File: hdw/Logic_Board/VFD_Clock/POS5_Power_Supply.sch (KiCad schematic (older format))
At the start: 0 parts

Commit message: Added +3.3V SW sheet
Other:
- note added: "LT8606? LT8607?"
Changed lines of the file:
@@
 EELAYER 29 0
 EELAYER END
-$Descr A4 11693 8268
+$Descr A 11000 8500
 encoding utf-8
-Sheet 1 21
+Sheet 20 22
 Title ""
 Date ""
@@
 Comment4 ""
 $EndDescr
+Text Notes 5040 3680 0    50   ~ 0
+LT8606? LT8607?
 $EndSCHEMATC

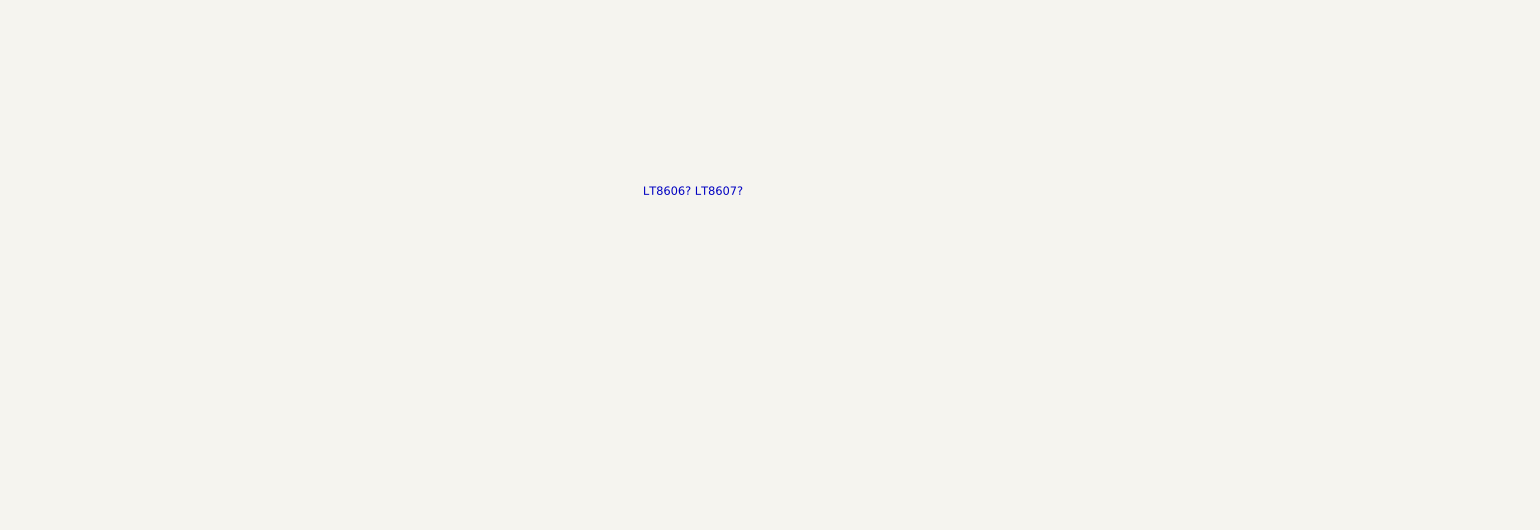
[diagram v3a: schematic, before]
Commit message: Power supply additions
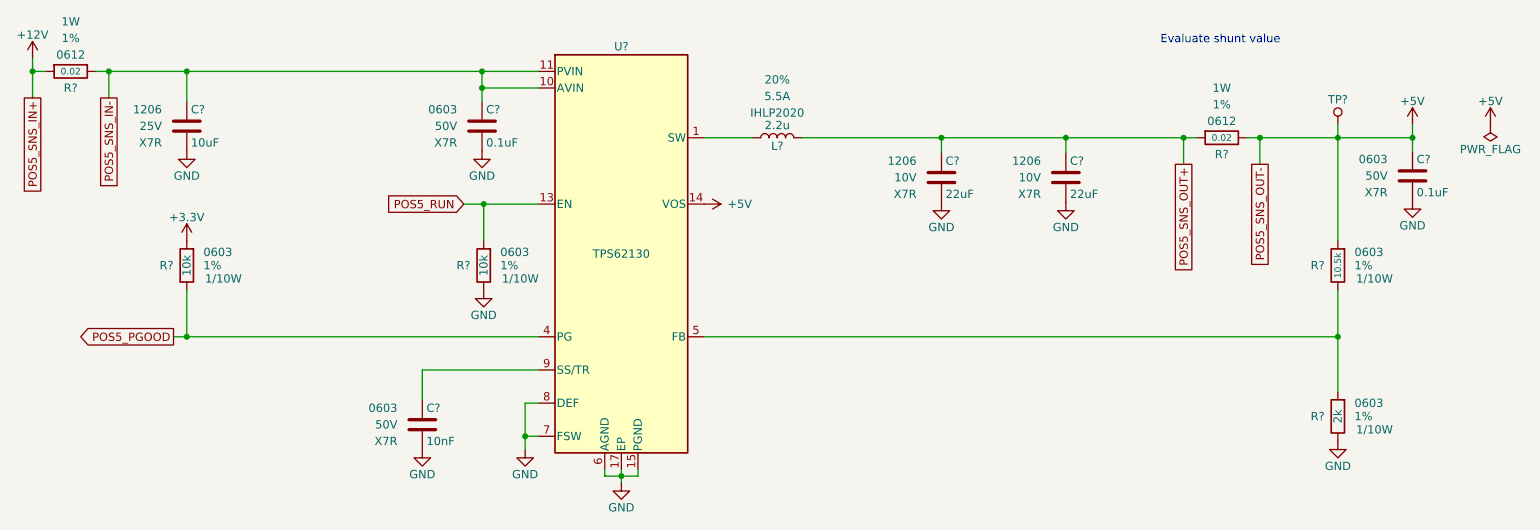
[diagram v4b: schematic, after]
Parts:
- added C? (x2): 0.1uF, Capacitors_SMD:C_0603, symbol Custom_Library:C_Custom
- added C?: 10uF, Capacitors_SMD:C_1206, symbol Custom_Library:C_Custom
- added C? (x2): 22uF, Capacitors_SMD:C_1206, symbol Custom_Library:C_Custom
- added C?: 10nF, Capacitors_SMD:C_0603, symbol Custom_Library:C_Custom
- added L?: 2.2u, Inductors_SMD:L_Vishay_IHLP-2020, symbol Custom_Library:L_Custom
- added R? (x2): 10k, Resistors_SMD:R_0603, symbol Custom_Library:R_Custom
- added R?: 2k, Resistors_SMD:R_0603, symbol Custom_Library:R_Custom
- added R? (x2): 0.02, Resistors_SMD:R_0612, symbol Custom_Library:R_Custom
- added R?: 10.5k, Resistors_SMD:R_0603, symbol Custom_Library:R_Custom
- added TP?: TP, Custom Footprints Library:Test_Point, symbol Custom_Library:TP
- added U?: TPS62130, Housings_DFN_QFN:QFN-16-1EP_3x3mm_Pitch0.5mm, symbol Custom_Library:TPS62130
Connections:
- new net: L?.1, U?.1 (SW), U?.2 (SW), U?.3 (SW)
- new net: R?.1, R?.2, U?.5 (FB)
- new net: C?.1, U?.9 (SS/TR)
- new net +12V: R?.1
- new net +3V3: R?.1
- new net +5V: C?.1, R?.1, R?.2, TP?.1 (TP), U?.14 (VOS)
- new net GND: C?.2, C?.2, C?.2, C?.2, C?.2, C?.2, R?.2, R?.2, U?.15 (PGND), U?.16 (PGND), U?.17 (EP), U?.6 (AGND), U?.7 (FSW), U?.8 (DEF)
- new net POS5_PGOOD: R?.2, U?.4 (PG)
- new net POS5_RUN: R?.1, U?.13 (EN)
- new net POS5_SNS_IN-: C?.1, C?.1, R?.2, U?.10 (AVIN), U?.11 (PVIN), U?.12 (PVIN)
- new net POS5_SNS_OUT+: C?.1, C?.1, L?.2, R?.1
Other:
- note added: "Evaluate shunt value"
- note removed: "LT8606? LT8607?"

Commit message: Changed to configurable discrete gates, added VBAT stuff
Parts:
- removed C?: 10uF, Capacitors_SMD:C_1206, symbol Custom_Library:C_Custom
- removed C? (x2): 22uF, Capacitors_SMD:C_1206, symbol Custom_Library:C_Custom
- removed C?: 0.1uF, Capacitors_SMD:C_0603, symbol Custom_Library:C_Custom
- removed L?: 2.2u, Inductors_SMD:L_Vishay_IHLP-2020, symbol Custom_Library:L_Custom
- removed R? (x2): 10k, Resistors_SMD:R_0603, symbol Custom_Library:R_Custom
- removed R? (x2): 0.02, Resistors_SMD:R_0612, symbol Custom_Library:R_Custom
- removed TP?: TP, Custom Footprints Library:Test_Point, symbol Custom_Library:TP
- removed U?: TPS62130, Housings_DFN_QFN:QFN-16-1EP_3x3mm_Pitch0.5mm, symbol Custom_Library:TPS62130
- added C?: 10uF, Capacitors_SMD:C_1206, symbol Custom_Library:C_Custom
- added C? (x2): 22uF, Capacitors_SMD:C_1206, symbol Custom_Library:C_Custom
- added C?: 0.1uF, Capacitors_SMD:C_0603, symbol Custom_Library:C_Custom
- added L?: 2.2u, Inductors_SMD:L_Vishay_IHLP-2020, symbol Custom_Library:L_Custom
- added R? (x2): 10k, Resistors_SMD:R_0603, symbol Custom_Library:R_Custom
- added R? (x2): 0.02, Resistors_SMD:R_0612, symbol Custom_Library:R_Custom
- added TP?: TP, Custom Footprints Library:Test_Point, symbol Custom_Library:TP
- added U?: TPS62130, Housings_DFN_QFN:QFN-16-1EP_3x3mm_Pitch0.5mm, symbol Custom_Library:TPS62130
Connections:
- net +12V: now also R?.1
- net +3V3: now also R?.1
- net +5V: now also C?.1, R?.2, TP?.1 (TP), U?.14 (VOS)
- net GND: now also C?.2, C?.2, C?.2, C?.2, R?.2, U?.15 (PGND), U?.16 (PGND), U?.17 (EP), U?.6 (AGND), U?.7 (FSW), U?.8 (DEF)
- net POS5_PGOOD: now also R?.2, U?.4 (PG)
- net POS5_RUN: now also R?.1, U?.13 (EN)
- net POS5_SNS_IN-: now also C?.1, R?.2, U?.10 (AVIN), U?.11 (PVIN), U?.12 (PVIN)
- net POS5_SNS_OUT+: now also C?.1, C?.1, L?.2, R?.1
- net at R?.1, R?.2: now also U?.5 (FB)
- net at C?.1: now also U?.9 (SS/TR)
- new net: L?.1, U?.1 (SW), U?.2 (SW), U?.3 (SW)
